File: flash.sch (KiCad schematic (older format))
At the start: 6 parts, among them U2101 MX25L1606E

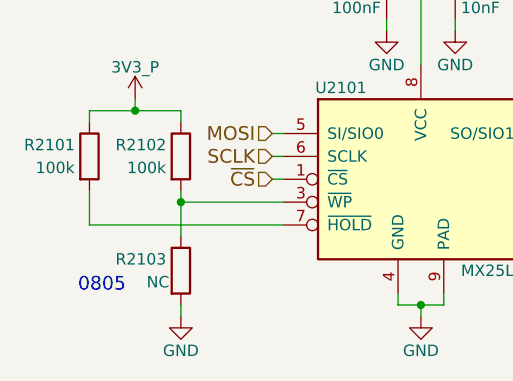
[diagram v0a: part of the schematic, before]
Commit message: Assign jumper header footprints and component properties, selected based on required current rating and minimized area occupied, assigned 1.5mm diameter test points
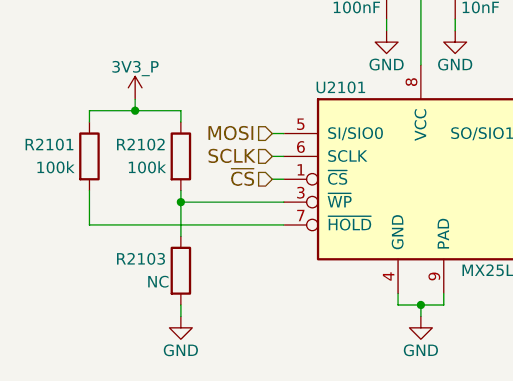
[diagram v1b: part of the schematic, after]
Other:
- note removed: "0805"
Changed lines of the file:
@@
 Wire Wire Line
 	4950 4300 4950 4250
-Text Notes 4500 4200 0    60   ~ 0
-0805
 $EndSCHEMATC

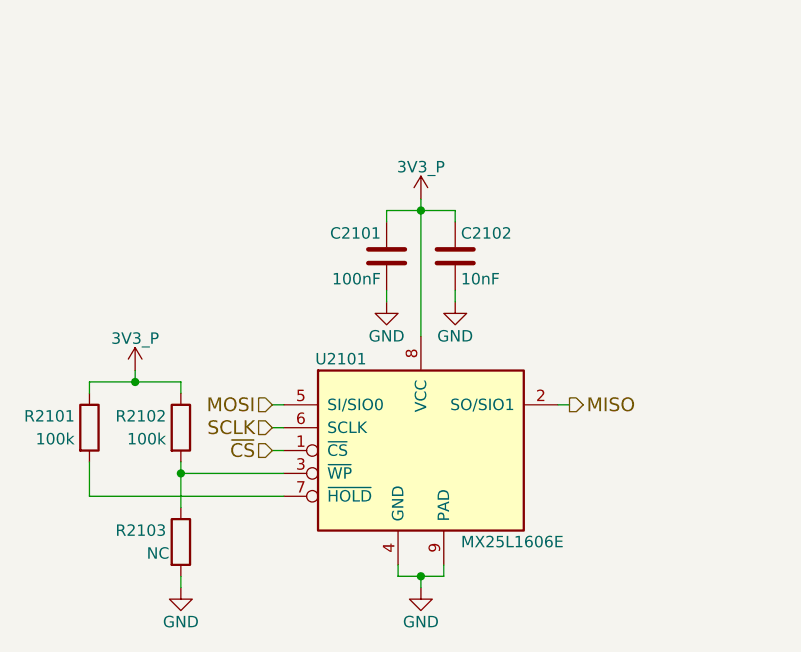
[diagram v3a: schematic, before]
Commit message: Move more symbols, sheets, and pins around on the front sheet to make it even clearer, bring back the old hierarchical structure (again), bring back each sheet's title, add large text "titles" to each sheet reflecting what they are for
Still need to double check everything on the first page.
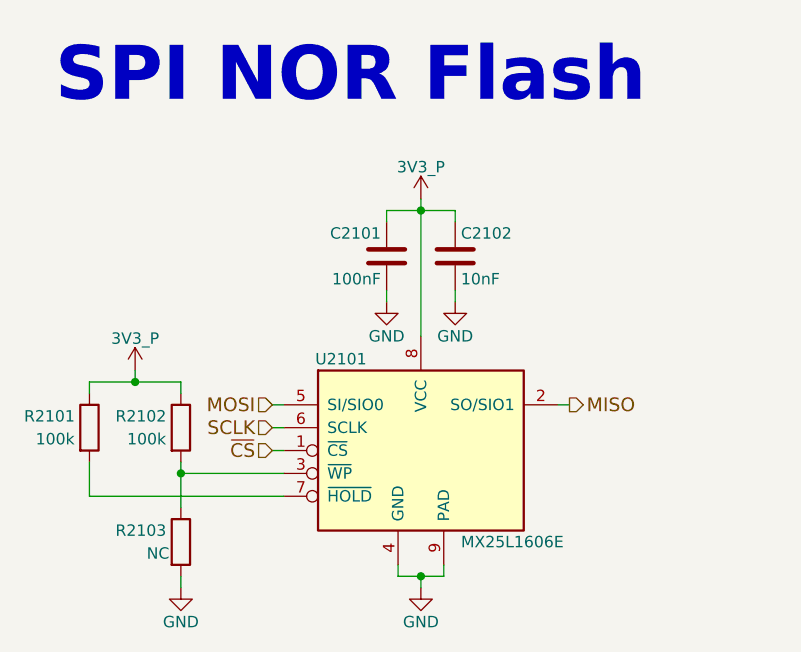
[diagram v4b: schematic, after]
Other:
- note added: "SPI NOR Flash"
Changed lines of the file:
@@
 encoding utf-8
 Sheet 21 24
-Title "Librem5 development kit"
+Title "SPI NOR Flash"
 Date "2018-06-11"
 Rev "v0.1.0"
@@
 $EndDescr
 $Comp
-L GND #PWR0243
+L GND #PWR0354
 U 1 1 5B12CD29
 P 6000 4300
-F 0 "#PWR0243" H 6000 4050 50  0001 C CNN
+F 0 "#PWR0354" H 6000 4050 50  0001 C CNN
 F 1 "GND" H 6000 4150 50  0000 C CNN
 F 2 "" H 6000 4300 50  0001 C CNN
@@
 $EndComp
 $Comp
-L 3V3_P #PWR0244
+L 3V3_P #PWR0355
 U 1 1 5B12EA15
 P 6000 2600
-F 0 "#PWR0244" H 6000 2450 50  0001 C CNN
+F 0 "#PWR0355" H 6000 2450 50  0001 C CNN
 F 1 "3V3_P" H 6000 2740 50  0000 C CNN
 F 2 "" H 6000 2600 50  0001 C CNN
@@
 $EndComp
 $Comp
-L GND #PWR0245
+L GND #PWR0356
 U 1 1 5B14F686
 P 5850 3050
-F 0 "#PWR0245" H 5850 2800 50  0001 C CNN
+F 0 "#PWR0356" H 5850 2800 50  0001 C CNN
 F 1 "GND" H 5850 2900 50  0000 C CNN
 F 2 "" H 5850 3050 50  0001 C CNN
@@
 $EndComp
 $Comp
-L GND #PWR0246
+L GND #PWR0357
 U 1 1 5B14F6A1
 P 6150 3050
-F 0 "#PWR0246" H 6150 2800 50  0001 C CNN
+F 0 "#PWR0357" H 6150 2800 50  0001 C CNN
 F 1 "GND" H 6150 2900 50  0000 C CNN
 F 2 "" H 6150 3050 50  0001 C CNN
@@
 $EndComp
 $Comp
-L 3V3_P #PWR0247
+L 3V3_P #PWR0358
 U 1 1 5B152DB7
 P 4750 3350
-F 0 "#PWR0247" H 4750 3200 50  0001 C CNN
+F 0 "#PWR0358" H 4750 3200 50  0001 C CNN
 F 1 "3V3_P" H 4750 3490 50  0000 C CNN
 F 2 "" H 4750 3350 50  0001 C CNN
@@
 Connection ~ 4950 3800
 $Comp
-L GND #PWR0248
+L GND #PWR0359
 U 1 1 5AFBA2C4
 P 4950 4300
-F 0 "#PWR0248" H 4950 4050 50  0001 C CNN
+F 0 "#PWR0359" H 4950 4050 50  0001 C CNN
 F 1 "GND" H 4950 4150 50  0000 C CNN
 F 2 "" H 4950 4300 50  0001 C CNN
@@
 Wire Wire Line
 	4950 4300 4950 4250
+Text Notes 4400 2200 0    236  ~ 47
+SPI NOR Flash
 $EndSCHEMATC

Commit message: Add AC coupling caps to the HDMI_AUXP/N diff pair which were mistakenly left out, fix a couple typos/errors that were made when transitioning to the new top-leve sheet, make the M.2s' I2C RX TX hierarchical signals consistent and clearer
Hopefully all lingering errors have been caught, this will likely be the schematic commit that gets reviewed (fingers crossed).
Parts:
- renumbered C2101 to C2001, C2102 to C2002, R2101 to R2001, R2102 to R2002, R2103 to R2003, U2101 to U2001
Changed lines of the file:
@@
 $Descr A4 11693 8268
 encoding utf-8
-Sheet 21 24
+Sheet 20 24
 Title "SPI NOR Flash"
 Date "2018-06-14"
@@
 $EndDescr
 $Comp
-L GND #PWR2105
+L GND #PWR0327
 U 1 1 5B12CD29
 P 6000 4300
-F 0 "#PWR2105" H 6000 4050 50  0001 C CNN
+F 0 "#PWR0327" H 6000 4050 50  0001 C CNN
 F 1 "GND" H 6000 4150 50  0000 C CNN
 F 2 "" H 6000 4300 50  0001 C CNN
@@
 $EndComp
 $Comp
-L MX25L1606E U2101
+L MX25L1606E U2001
 U 1 1 5B12CFC8
 P 6000 3700
-F 0 "U2101" H 5650 4100 50  0000 C CNN
+F 0 "U2001" H 5650 4100 50  0000 C CNN
 F 1 "MX25L1606E" H 6400 3300 50  0000 C CNN
 F 2 "Housings_DFN_QFN:DFN-S-8-1EP_6x5mm_Pitch1.27mm" H 6800 3800 50  0001 C CNN
@@
 $EndComp
 $Comp
-L 3V3_P #PWR2104
+L 3V3_P #PWR0328
 U 1 1 5B12EA15
 P 6000 2600
-F 0 "#PWR2104" H 6000 2450 50  0001 C CNN
+F 0 "#PWR0328" H 6000 2450 50  0001 C CNN
 F 1 "3V3_P" H 6000 2740 50  0000 C CNN
 F 2 "" H 6000 2600 50  0001 C CNN
@@
 $EndComp
 $Comp
-L C C2101
+L C C2001
 U 1 1 5B12EA2B
 P 5850 2850
-F 0 "C2101" H 5875 2950 50  0000 L CNN
+F 0 "C2001" H 5875 2950 50  0000 L CNN
 F 1 "100nF" H 5875 2750 50  0000 L CNN
 F 2 "Capacitors_SMD:C_0603" H 5888 2700 50  0001 C CNN
@@
 $EndComp
 $Comp
-L C C2102
+L C C2002
 U 1 1 5B14E905
 P 6150 2850
-F 0 "C2102" H 6175 2950 50  0000 L CNN
+F 0 "C2002" H 6175 2950 50  0000 L CNN
 F 1 "10nF" H 6175 2750 50  0000 L CNN
 F 2 "Capacitors_SMD:C_0603" H 6188 2700 50  0001 C CNN
@@
 $EndComp
 $Comp
-L GND #PWR2103
+L GND #PWR0329
 U 1 1 5B14F686
 P 5850 3050
-F 0 "#PWR2103" H 5850 2800 50  0001 C CNN
+F 0 "#PWR0329" H 5850 2800 50  0001 C CNN
 F 1 "GND" H 5850 2900 50  0000 C CNN
 F 2 "" H 5850 3050 50  0001 C CNN
@@
 $EndComp
 $Comp
-L GND #PWR2106
+L GND #PWR0330
 U 1 1 5B14F6A1
 P 6150 3050
-F 0 "#PWR2106" H 6150 2800 50  0001 C CNN
+F 0 "#PWR0330" H 6150 2800 50  0001 C CNN
 F 1 "GND" H 6150 2900 50  0000 C CNN
 F 2 "" H 6150 3050 50  0001 C CNN
@@
 ~CS
 $Comp
-L R R2101
+L R R2001
 U 1 1 5B152CDF
 P 4550 3600
-F 0 "R2101" H 4375 3650 50  0000 C CNN
+F 0 "R2001" H 4375 3650 50  0000 C CNN
 F 1 "100k" H 4400 3550 50  0000 C CNN
 F 2 "Resistors_SMD:R_0603" V 4480 3600 50  0001 C CNN
@@
 $EndComp
 $Comp
-L 3V3_P #PWR2101
+L 3V3_P #PWR0331
 U 1 1 5B152DB7
 P 4750 3350
-F 0 "#PWR2101" H 4750 3200 50  0001 C CNN
+F 0 "#PWR0331" H 4750 3200 50  0001 C CNN
 F 1 "3V3_P" H 4750 3490 50  0000 C CNN
 F 2 "" H 4750 3350 50  0001 C CNN
@@
 $EndComp
 $Comp
-L R R2102
+L R R2002
 U 1 1 5AFB92E3
 P 4950 3600
-F 0 "R2102" H 4775 3650 50  0000 C CNN
+F 0 "R2002" H 4775 3650 50  0000 C CNN
 F 1 "100k" H 4800 3550 50  0000 C CNN
 F 2 "Resistors_SMD:R_0603" V 4880 3600 50  0001 C CNN
@@
 $EndComp
 $Comp
-L R R2103
+L R R2003
 U 1 1 5AFBA0EE
 P 4950 4100
-F 0 "R2103" H 4775 4150 50  0000 C CNN
+F 0 "R2003" H 4775 4150 50  0000 C CNN
 F 1 "NC" H 4850 4050 50  0000 C CNN
 F 2 "Resistors_SMD:R_0603" V 4880 4100 50  0001 C CNN
@@
 Connection ~ 4950 3800
 $Comp
-L GND #PWR2102
+L GND #PWR0332
 U 1 1 5AFBA2C4
 P 4950 4300
-F 0 "#PWR2102" H 4950 4050 50  0001 C CNN
+F 0 "#PWR0332" H 4950 4050 50  0001 C CNN
 F 1 "GND" H 4950 4150 50  0000 C CNN
 F 2 "" H 4950 4300 50  0001 C CNN

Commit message: Move the WLAN+BT M.2 sheet back to page 18 rather than the last page (24)
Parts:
- renumbered C2001 to C2101, C2002 to C2102, R2001 to R2101, R2002 to R2102, R2003 to R2103, U2001 to U2101
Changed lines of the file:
@@
 $Descr A4 11693 8268
 encoding utf-8
-Sheet 20 24
+Sheet 21 24
 Title "SPI NOR Flash"
-Date "2018-06-14"
+Date "2018-06-15"
 Rev "v0.1.0"
 Comp "Copyright 2018 GNU GPLv3"
@@
 $EndDescr
 $Comp
-L GND #PWR0327
+L GND #PWR0353
 U 1 1 5B12CD29
 P 6000 4300
-F 0 "#PWR0327" H 6000 4050 50  0001 C CNN
+F 0 "#PWR0353" H 6000 4050 50  0001 C CNN
 F 1 "GND" H 6000 4150 50  0000 C CNN
 F 2 "" H 6000 4300 50  0001 C CNN
@@
 $EndComp
 $Comp
-L MX25L1606E U2001
+L MX25L1606E U2101
 U 1 1 5B12CFC8
 P 6000 3700
-F 0 "U2001" H 5650 4100 50  0000 C CNN
+F 0 "U2101" H 5650 4100 50  0000 C CNN
 F 1 "MX25L1606E" H 6400 3300 50  0000 C CNN
 F 2 "Housings_DFN_QFN:DFN-S-8-1EP_6x5mm_Pitch1.27mm" H 6800 3800 50  0001 C CNN
@@
 $EndComp
 $Comp
-L 3V3_P #PWR0328
+L 3V3_P #PWR0354
 U 1 1 5B12EA15
 P 6000 2600
-F 0 "#PWR0328" H 6000 2450 50  0001 C CNN
+F 0 "#PWR0354" H 6000 2450 50  0001 C CNN
 F 1 "3V3_P" H 6000 2740 50  0000 C CNN
 F 2 "" H 6000 2600 50  0001 C CNN
@@
 $EndComp
 $Comp
-L C C2001
+L C C2101
 U 1 1 5B12EA2B
 P 5850 2850
-F 0 "C2001" H 5875 2950 50  0000 L CNN
+F 0 "C2101" H 5875 2950 50  0000 L CNN
 F 1 "100nF" H 5875 2750 50  0000 L CNN
 F 2 "Capacitors_SMD:C_0603" H 5888 2700 50  0001 C CNN
@@
 $EndComp
 $Comp
-L C C2002
+L C C2102
 U 1 1 5B14E905
 P 6150 2850
-F 0 "C2002" H 6175 2950 50  0000 L CNN
+F 0 "C2102" H 6175 2950 50  0000 L CNN
 F 1 "10nF" H 6175 2750 50  0000 L CNN
 F 2 "Capacitors_SMD:C_0603" H 6188 2700 50  0001 C CNN
@@
 $EndComp
 $Comp
-L GND #PWR0329
+L GND #PWR0355
 U 1 1 5B14F686
 P 5850 3050
-F 0 "#PWR0329" H 5850 2800 50  0001 C CNN
+F 0 "#PWR0355" H 5850 2800 50  0001 C CNN
 F 1 "GND" H 5850 2900 50  0000 C CNN
 F 2 "" H 5850 3050 50  0001 C CNN
@@
 $EndComp
 $Comp
-L GND #PWR0330
+L GND #PWR0356
 U 1 1 5B14F6A1
 P 6150 3050
-F 0 "#PWR0330" H 6150 2800 50  0001 C CNN
+F 0 "#PWR0356" H 6150 2800 50  0001 C CNN
 F 1 "GND" H 6150 2900 50  0000 C CNN
 F 2 "" H 6150 3050 50  0001 C CNN
@@
 ~CS
 $Comp
-L R R2001
+L R R2101
 U 1 1 5B152CDF
 P 4550 3600
-F 0 "R2001" H 4375 3650 50  0000 C CNN
+F 0 "R2101" H 4375 3650 50  0000 C CNN
 F 1 "100k" H 4400 3550 50  0000 C CNN
 F 2 "Resistors_SMD:R_0603" V 4480 3600 50  0001 C CNN
@@
 $EndComp
 $Comp
-L 3V3_P #PWR0331
+L 3V3_P #PWR0357
 U 1 1 5B152DB7
 P 4750 3350
-F 0 "#PWR0331" H 4750 3200 50  0001 C CNN
+F 0 "#PWR0357" H 4750 3200 50  0001 C CNN
 F 1 "3V3_P" H 4750 3490 50  0000 C CNN
 F 2 "" H 4750 3350 50  0001 C CNN
@@
 $EndComp
 $Comp
-L R R2002
+L R R2102
 U 1 1 5AFB92E3
 P 4950 3600
-F 0 "R2002" H 4775 3650 50  0000 C CNN
+F 0 "R2102" H 4775 3650 50  0000 C CNN
 F 1 "100k" H 4800 3550 50  0000 C CNN
 F 2 "Resistors_SMD:R_0603" V 4880 3600 50  0001 C CNN
@@
 $EndComp
 $Comp
-L R R2003
+L R R2103
 U 1 1 5AFBA0EE
 P 4950 4100
-F 0 "R2003" H 4775 4150 50  0000 C CNN
+F 0 "R2103" H 4775 4150 50  0000 C CNN
 F 1 "NC" H 4850 4050 50  0000 C CNN
 F 2 "Resistors_SMD:R_0603" V 4880 4100 50  0001 C CNN
@@
 Connection ~ 4950 3800
 $Comp
-L GND #PWR0332
+L GND #PWR0358
 U 1 1 5AFBA2C4
 P 4950 4300
-F 0 "#PWR0332" H 4950 4050 50  0001 C CNN
+F 0 "#PWR0358" H 4950 4050 50  0001 C CNN
 F 1 "GND" H 4950 4150 50  0000 C CNN
 F 2 "" H 4950 4300 50  0001 C CNN
